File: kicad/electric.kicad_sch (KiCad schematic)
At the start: 4 parts

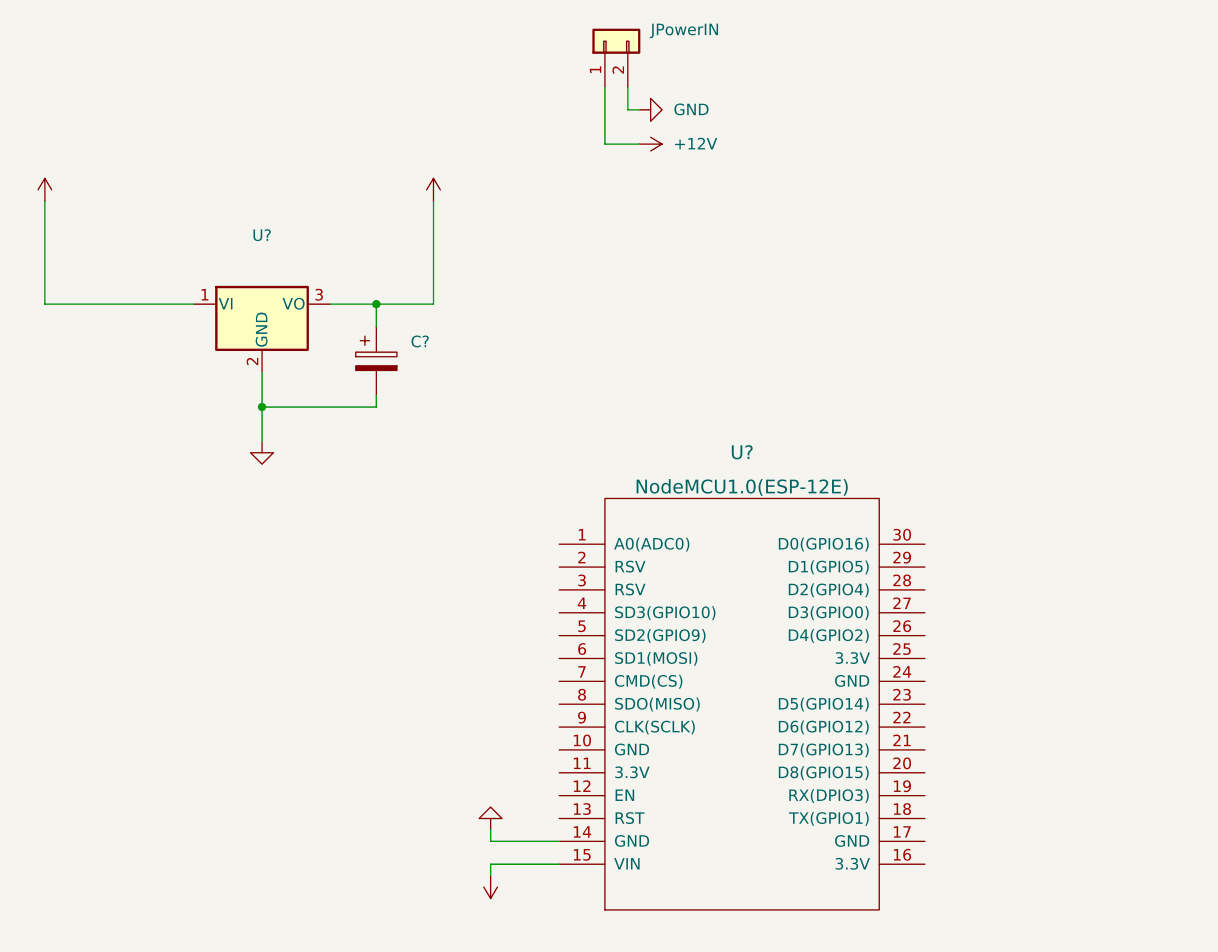
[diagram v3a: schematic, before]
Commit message: feat(kicad): added fan output
Signed-off-by: Mario-F <github@fritschen.net>
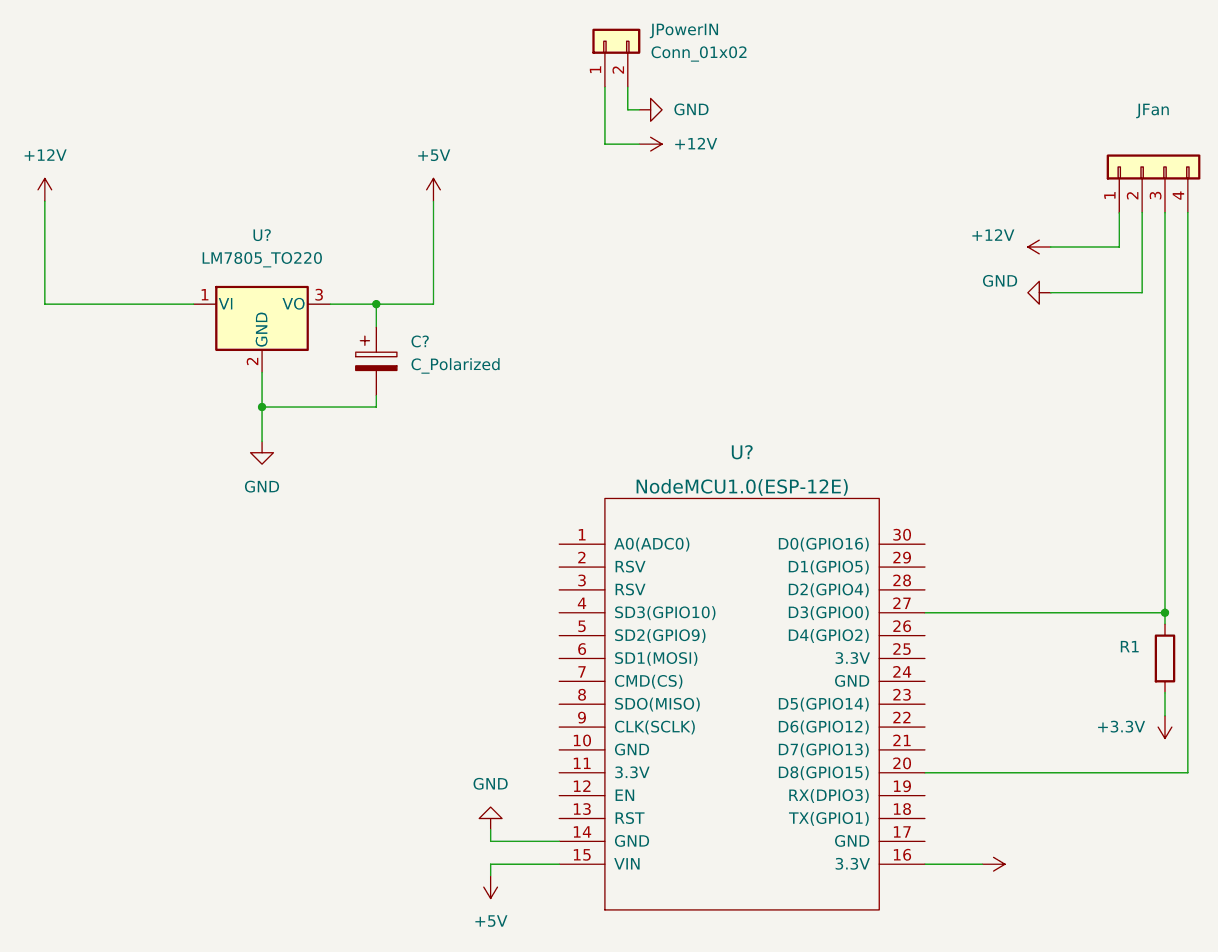
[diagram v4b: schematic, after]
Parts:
- added JFan: (no value), symbol Connector_Generic:Conn_01x04
- added R1: (no value), symbol Device:R
- C?: value (none) -> C_Polarized
- JPowerIN: value (none) -> Conn_01x02
- U?: value (none) -> LM7805_TO220; footprint (none) -> Package_TO_SOT_THT:TO-220-3_Vertical
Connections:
- net +12V: now also JFan.1 (Pin_1)
- net GND: now also JFan.2 (Pin_2)
- net +3V3: now reaches U?.16 (3.3V)
- net +3V3: now also R1.2
- net at U?.20 (D8(GPIO15)): now also JFan.4 (Pin_4)
- net at U?.27 (D3(GPIO0)): now also JFan.3 (Pin_3), R1.1

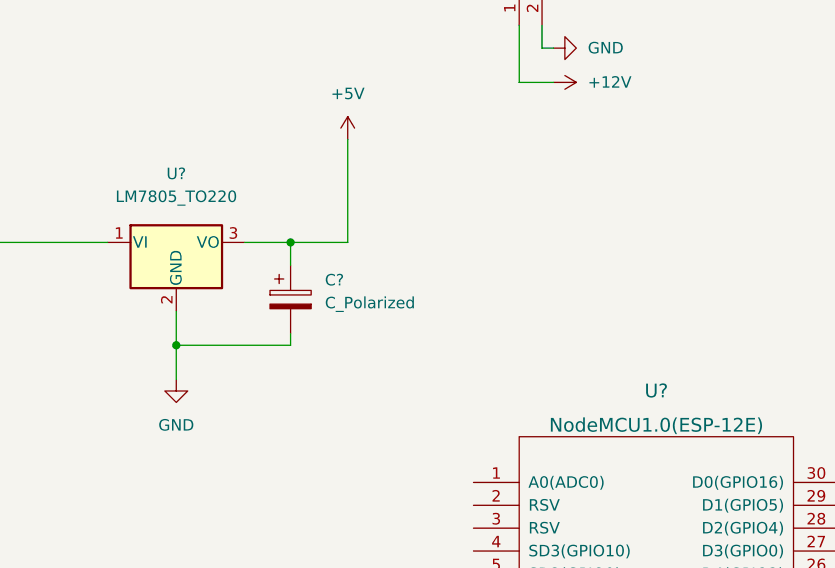
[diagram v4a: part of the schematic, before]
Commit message: fix(kicad): name unnamed devices
Signed-off-by: Mario-F <github@fritschen.net>
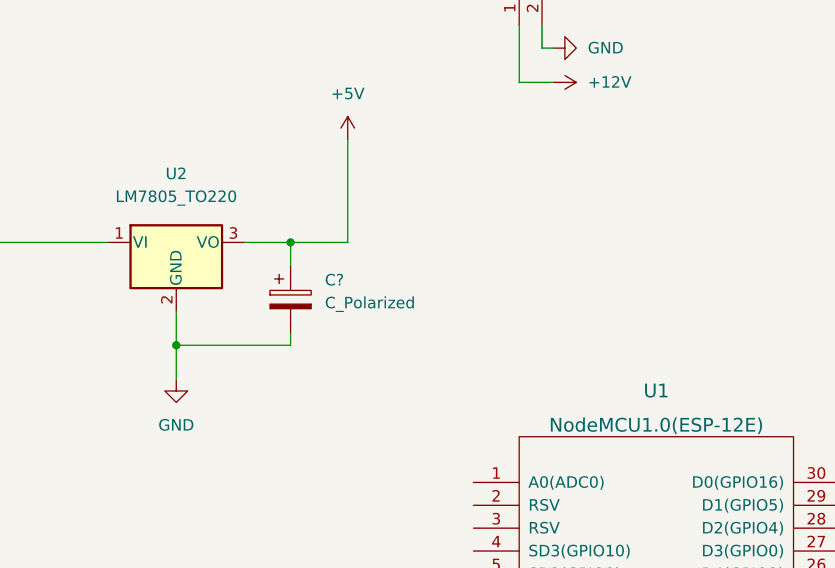
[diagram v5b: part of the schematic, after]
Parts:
- gave numbers to parts that had none: 2
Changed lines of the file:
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@@
   (symbol (lib_id "ESP8266:NodeMCU1.0(ESP-12E)") (at 140.97 95.25 0) (unit 1)
     (in_bom yes) (on_board yes) (fields_autoplaced)
-    (property "Reference" "U?" (id 0) (at 140.97 67.31 0)
+    (property "Reference" "U1" (id 0) (at 140.97 67.31 0)
       (effects (font (size 1.524 1.524)))
     )
@@
   (symbol (lib_id "Regulator_Linear:LM7805_TO220") (at 87.63 50.8 0) (unit 1)
     (in_bom yes) (on_board yes) (fields_autoplaced)
-    (property "Reference" "U?" (id 0) (at 87.63 43.18 0))
+    (property "Reference" "U2" (id 0) (at 87.63 43.18 0))
     (property "Value" "LM7805_TO220" (id 1) (at 87.63 45.72 0))
     (property "Footprint" "Package_TO_SOT_THT:TO-220-3_Vertical" (id 2) (at 87.63 45.085 0)
@@
     )
     (path "/4244f2cf-53fb-48c6-88ac-de581a83aeb5"
-      (reference "U?") (unit 1) (value "NodeMCU1.0(ESP-12E)") (footprint "")
+      (reference "U1") (unit 1) (value "NodeMCU1.0(ESP-12E)") (footprint "")
     )
     (path "/e997c615-0a9d-46fc-872f-6b2d14f01b36"
-      (reference "U?") (unit 1) (value "LM7805_TO220") (footprint "Package_TO_SOT_THT:TO-220-3_Vertical")
-    )
-  )
+      (reference "U2") (unit 1) (value "LM7805_TO220") (footprint "Package_TO_SOT_THT:TO-220-3_Vertical")
+    )
+  )

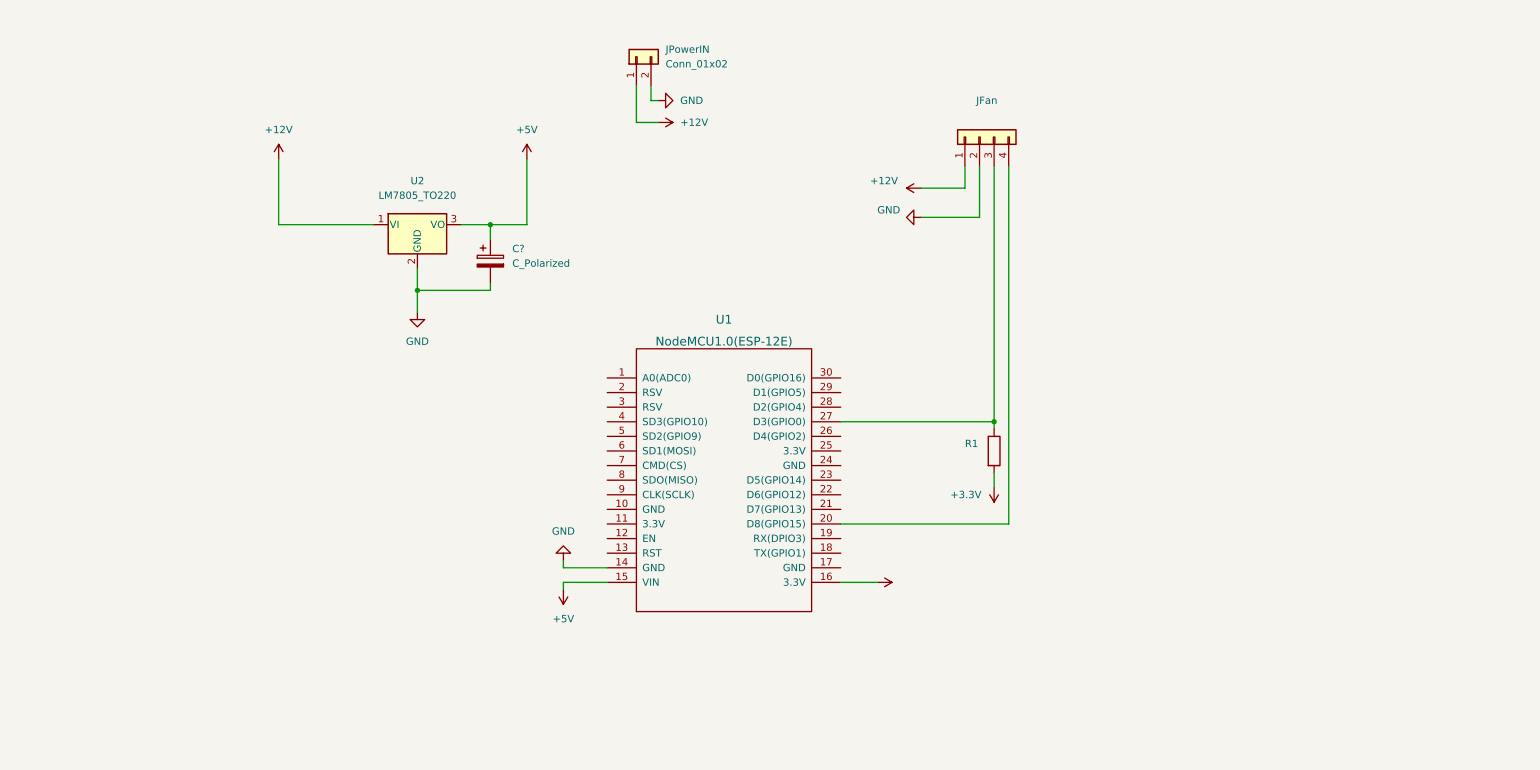
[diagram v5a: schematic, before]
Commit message: feat(kicad): added temp sensor circut
Signed-off-by: Mario-F <github@fritschen.net>
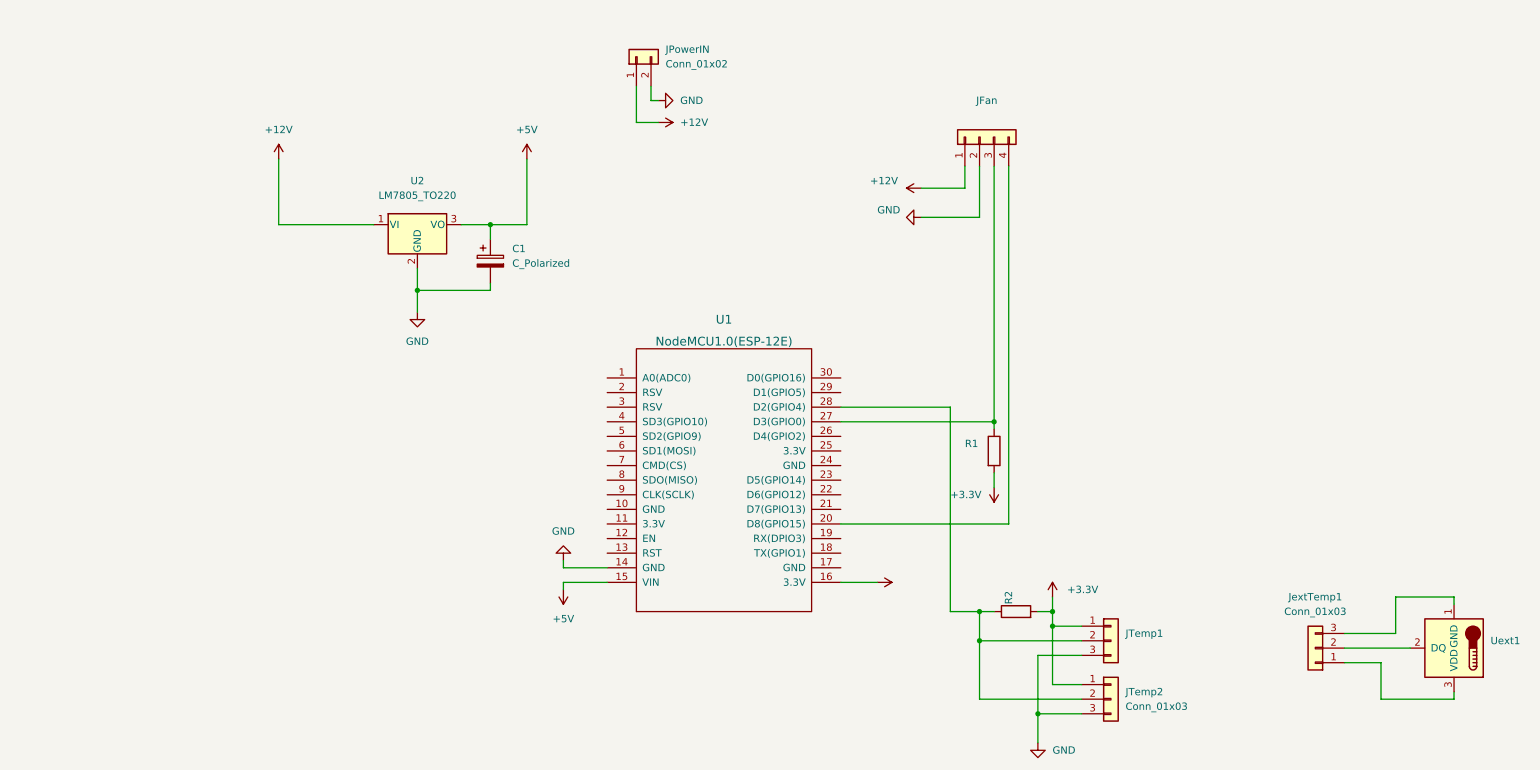
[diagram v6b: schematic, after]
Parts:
- added JTemp1: (no value), symbol Connector_Generic:Conn_01x03
- added JTemp2, JextTemp1: Conn_01x03, symbol Connector_Generic:Conn_01x03
- added R2: (no value), symbol Device:R
- added Uext1: (no value), symbol Sensor_Temperature:DS18B20
- gave numbers to parts that had none: 1
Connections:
- net +3V3: now also JTemp1.1 (Pin_1), JTemp2.1 (Pin_1), R2.2
- net GND: now also JTemp1.3 (Pin_3), JTemp2.3 (Pin_3)
- net at U1.28 (D2(GPIO4)): now also JTemp1.2 (Pin_2), JTemp2.2 (Pin_2), R2.1
- new net: JextTemp1.1 (Pin_1), Uext1.3 (VDD)
- new net: JextTemp1.2 (Pin_2), Uext1.2 (DQ)
- new net: JextTemp1.3 (Pin_3), Uext1.1 (GND)

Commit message: feat(kicad): tidy up shematic
Signed-off-by: Mario-F <github@fritschen.net>
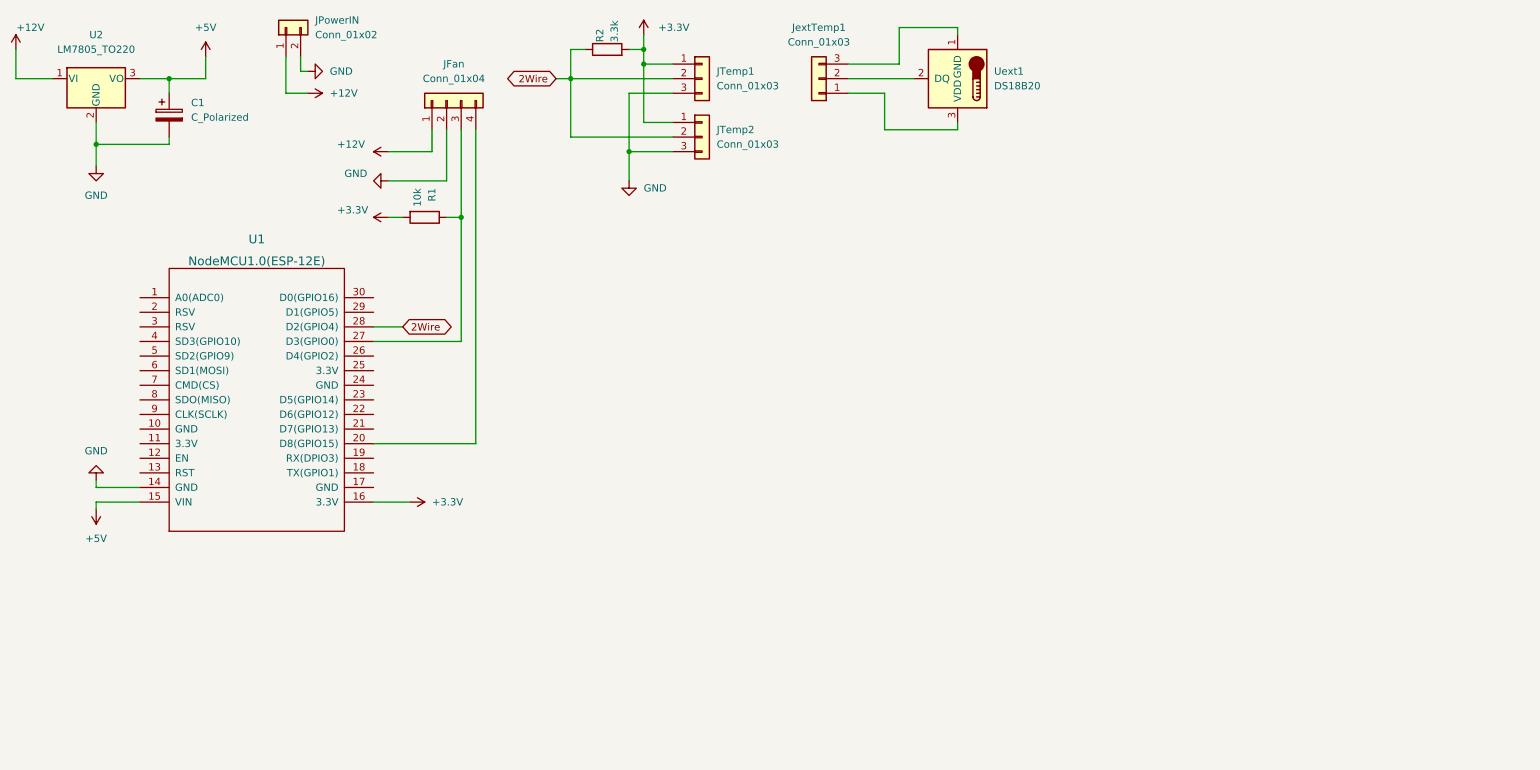
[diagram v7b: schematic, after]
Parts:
- JFan: value (none) -> Conn_01x04
- JTemp1: value (none) -> Conn_01x03
- R1: value (none) -> 10k
- R2: value (none) -> 3.3k
- Uext1: value (none) -> DS18B20; footprint (none) -> Package_TO_SOT_THT:TO-92_Inline
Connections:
- net 2Wire: now reaches JTemp1.2 (Pin_2), JTemp2.2 (Pin_2), R2.1, U1.28 (D2(GPIO4))
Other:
- title: (none) -> ESP Temp and Fancontroller
- moved on the sheet: C1, JFan, JPowerIN, JTemp1, JTemp2, JextTemp1, R1, R2, U1, U2, Uext1

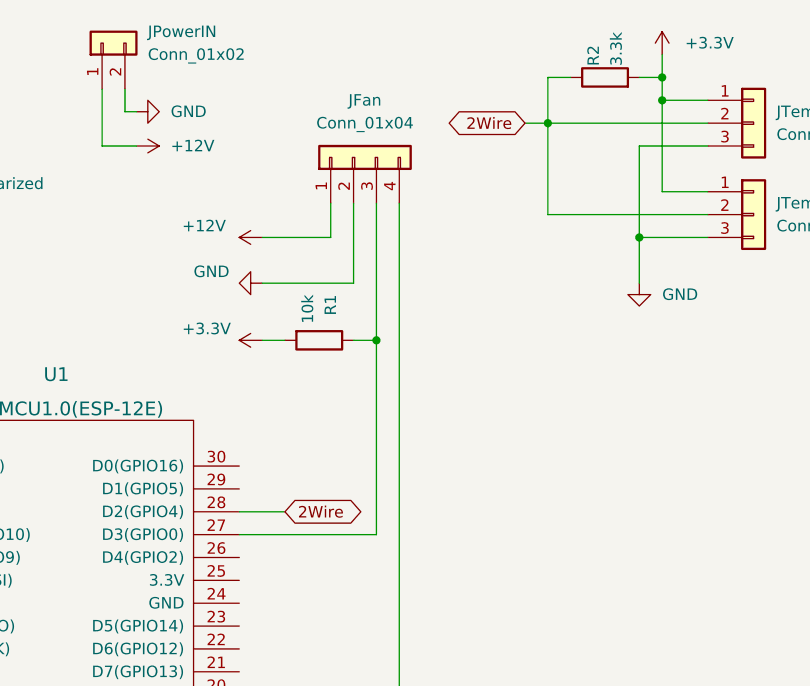
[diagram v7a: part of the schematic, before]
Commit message: fix(kicad): named 1wire 2wire
Signed-off-by: Mario-F <github@fritschen.net>
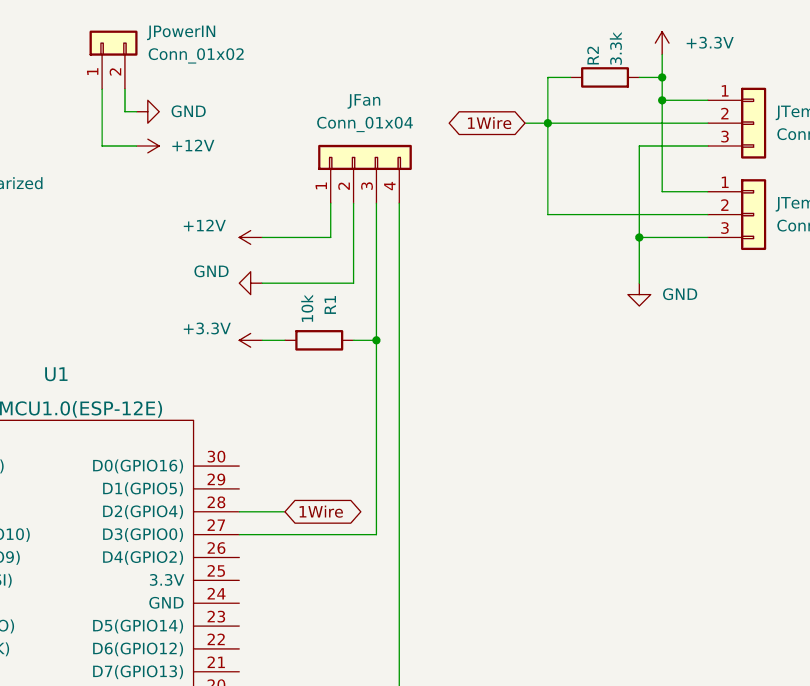
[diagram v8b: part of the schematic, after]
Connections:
- net 2Wire renamed 1Wire
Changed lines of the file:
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@@
     (stroke (width 0) (type default) (color 0 0 0 0))
   )
-  (global_label "2Wire" (shape bidirectional) (at 85.09 68.58 0) (fields_autoplaced)
+  (global_label "1Wire" (shape bidirectional) (at 85.09 68.58 0) (fields_autoplaced)
     (effects (font (size 1.27 1.27)) (justify left))
-    (property "Intersheet References" "${INTERSHEET_REFS}" (id 0) (at 92.6436 68.6594 0)
+    (property "Intersheet References" "${INTERSHEET_REFS}" (id 0) (at 92.6436 68.5006 0)
       (effects (font (size 1.27 1.27)) (justify left) hide)
     )
   )
-  (global_label "2Wire" (shape bidirectional) (at 111.76 25.4 180) (fields_autoplaced)
+  (global_label "1Wire" (shape bidirectional) (at 111.76 25.4 180) (fields_autoplaced)
     (effects (font (size 1.27 1.27)) (justify right))
     (property "Intersheet References" "${INTERSHEET_REFS}" (id 0) (at 104.2064 25.3206 0)
